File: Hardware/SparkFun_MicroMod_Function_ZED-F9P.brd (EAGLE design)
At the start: 38 x 65 mm, 126 parts, among them J2 MICROMOD_STANDARD, J3 QWIIC_RA, J4 U.FL, Q1 DMP21D0UT, U1 EEPROM, U2 U-BLOX_ZED-F9P, U3 FIN1017MXSOIC-8, U4 SN74AUP1T04DCK, U5 PCA9306DCUR, U6 74LVC541ABQ, U7 MIC5219 3.3V, U8 MIC5219 3.3V, U9 74LVC541ABQ

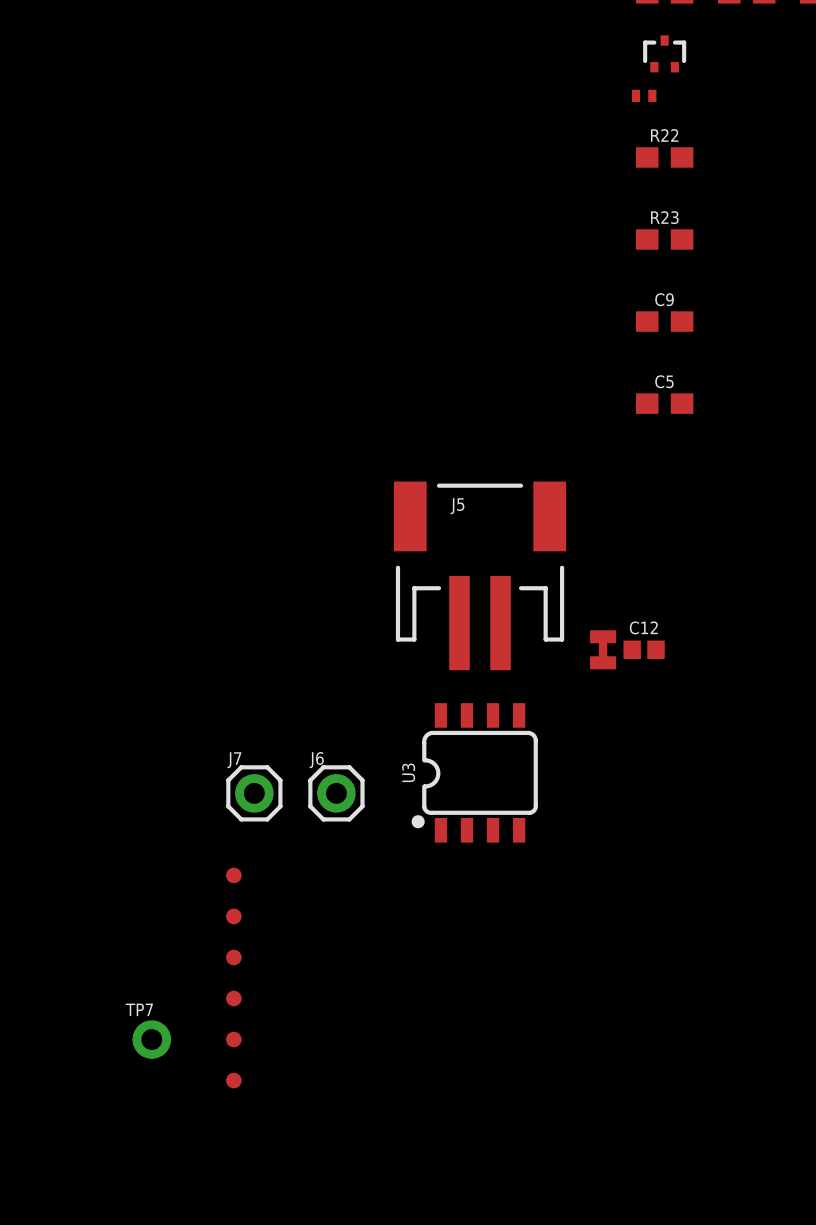
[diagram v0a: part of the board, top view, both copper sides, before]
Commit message: Changed power resistor, needed higher power rating.
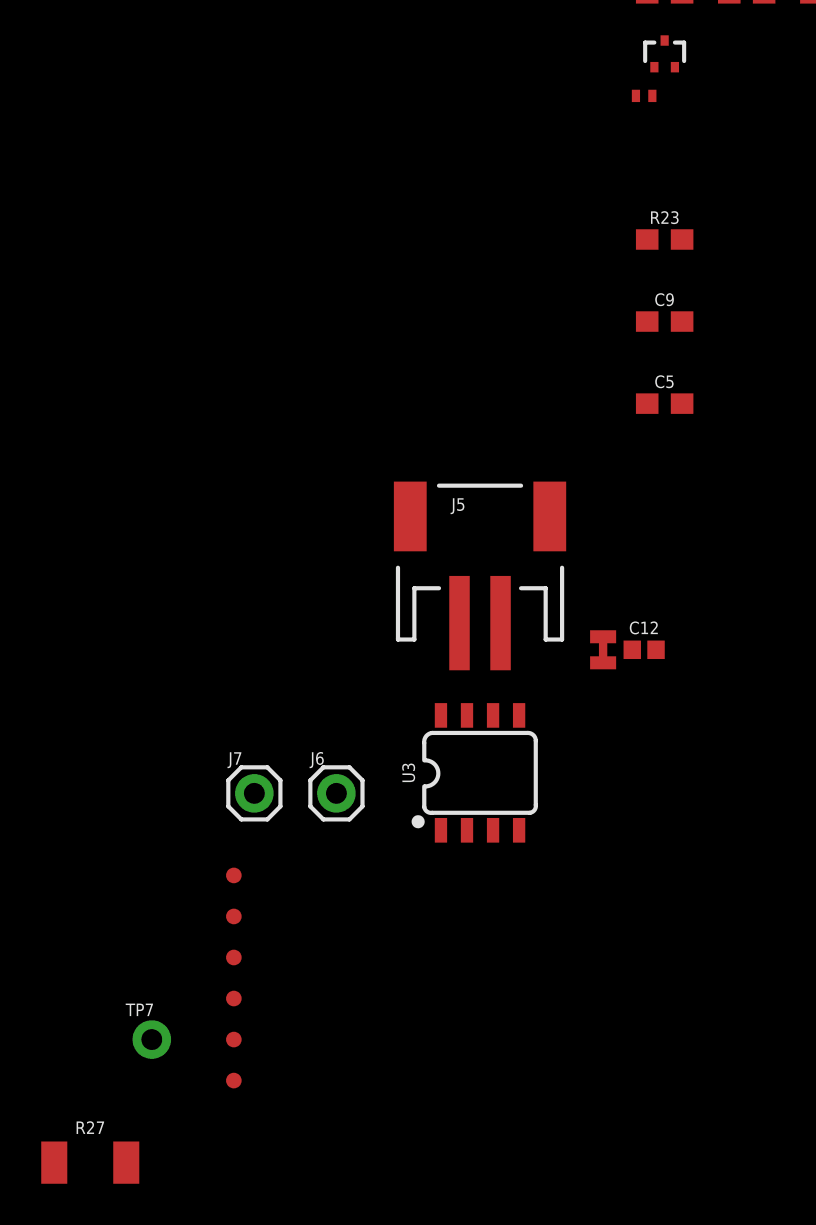
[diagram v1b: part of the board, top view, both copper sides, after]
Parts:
- removed R22: 20, SparkFun-Resistors:0603
- added R27: RK73H2ETTD16R9F, MicroMod_Function_GNSS_ublox_ZED_F9P:1210
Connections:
- net ANT_!SHORT!: now also R27.1; no longer R22.1
- net N$49: now also R27.2; no longer R22.2
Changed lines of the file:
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@@
 <attribute name="INDUCTANCE" value="150nH" x="-55" y="-966" size="1.778" layer="27" display="off"/>
-</element>
-<element name="R22" library="SparkFun-Resistors" package="0603" value="20" x="-54" y="-969" smashed="yes">
-<attribute name="NAME" x="-54" y="-968.238" size="0.6096" layer="25" font="vector" ratio="20" align="bottom-center"/>
-<attribute name="PROD_ID" value="RES-07862" x="-54" y="-969" size="1.778" layer="27" display="off"/>
-<attribute name="VALUE" x="-54" y="-969.762" size="0.6096" layer="27" font="vector" ratio="20" align="top-center"/>
 </element>
 <element name="R23" library="SparkFun-Resistors" package="0603" value="2.0k" x="-54" y="-973" smashed="yes">
@@
 <element name="TP19" library="SparkFun-Connectors" package="PAD.03X.03" value="TEST-POINT3" x="-83" y="141" smashed="yes"/>
 <element name="TP20" library="SparkFun-Connectors" package="PAD.03X.03" value="TEST-POINT3" x="-83" y="144" smashed="yes"/>
+<element name="R27" library="MicroMod_Function_GNSS_ublox_ZED_F9P" package="1210" value="RK73H2ETTD16R9F" x="-82" y="-1018" smashed="yes">
+<attribute name="NAME" x="-82" y="-1016.603" size="0.6096" layer="25" font="vector" ratio="20" align="bottom-center"/>
+<attribute name="POWER" value="0.5W" x="-82" y="-1018" size="1.778" layer="27" display="off"/>
+<attribute name="RESISTANCE" value="16.9" x="-82" y="-1018" size="1.778" layer="27" display="off"/>
+<attribute name="TOLERANCE" value="1%" x="-82" y="-1018" size="1.778" layer="27" display="off"/>
+<attribute name="VALUE" x="-82" y="-1019.397" size="0.6096" layer="27" font="vector" ratio="20" align="top-center"/>
+</element>
 </elements>
 <signals>
@@
 <contactref element="U6" pad="P$8"/>
 <contactref element="Q1" pad="P$1"/>
-<contactref element="R22" pad="1"/>
 <contactref element="R23" pad="2"/>
-<wire x1="-54.85" y1="-969" x2="-53.15" y2="-973" width="0" layer="19" extent="1-1"/>
-<wire x1="-54" y1="-963.3" x2="-54.85" y2="-969" width="0" layer="19" extent="1-1"/>
+<contactref element="R27" pad="1"/>
+<wire x1="-53.15" y1="-973" x2="-83.755" y2="-1018" width="0" layer="19" extent="1-1"/>
+<wire x1="-54" y1="-963.3" x2="-53.15" y2="-973" width="0" layer="19" extent="1-1"/>
 <wire x1="-28.75" y1="-480.35" x2="-54" y2="-963.3" width="0" layer="19" extent="1-1"/>
 </signal>
@@
 <contactref element="C13" pad="1"/>
 <contactref element="L1" pad="P$1"/>
-<contactref element="R22" pad="2"/>
+<contactref element="R27" pad="2"/>
 <wire x1="-43.5" y1="-961" x2="-52.05" y2="-955.6999" width="0" layer="19" extent="1-1"/>
 <wire x1="-55.4" y1="-966" x2="-52.05" y2="-955.6999" width="0" layer="19" extent="1-1"/>
-<wire x1="-53.15" y1="-969" x2="-55.4" y2="-966" width="0" layer="19" extent="1-1"/>
+<wire x1="-80.245" y1="-1018" x2="-55.4" y2="-966" width="0" layer="19" extent="1-1"/>
 </signal>
 <signal name="N$14">

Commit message: Update Post schematic review.
Made all easy changes, in midst of redoing decoupling per requests.
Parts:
- removed BYP, JP7, USB_EN: JUMPER-SMT_2_NO_SILK, SparkFun-Jumpers:SMT-JUMPER_2_NO_SILK
- removed C3, C5: 470pF, SparkFun-Capacitors:0603
- removed C4, C6: 2.2uF, SparkFun-Capacitors:0603
- removed D1, D12, D2, D8: RED, SparkFun-LED:LED-0603
- removed D10: 3A/10V/280mV, SparkFun-DiscreteSemi:SOD-323
- removed F1: 6V/2A, SparkFun-Fuses:1210
- removed JP10, JP2, JP3, JP8: JUMPER-SMT_2_NC_TRACE_SILK, SparkFun-Jumpers:SMT-JUMPER_2_NC_TRACE_SILK
- removed JP11, JP12: (no value), SparkFun-Jumpers:SMT-JUMPER_3_2-NC_TRACE_SILK
- removed R13, R14, R15, R16: 1.5k, SparkFun-Resistors:0603
- removed R17: 100k, SparkFun-Resistors:0603
- removed R19, R21, R4: 1k, SparkFun-Resistors:0603
- removed U$3, U$7: OPA344, SparkFun-IC-Amplifiers:SOT23-5
- removed U7, U8: MIC5219 3.3V, SparkFun-IC-Power:SOT23-5
- added C18: 2.2uF, SparkFun-Capacitors:0402-TIGHT
- added C19, C20: 0.1uF, SparkFun-Capacitors:0603
- added J8: Bus Selection, SparkFun-Connectors:1X03_LOCK
- added J9: (no value), SparkFun-Connectors:1X02
- added JP13: JUMPER-SMT_2_NO_SILK, SparkFun-Jumpers:SMT-JUMPER_2_NO_SILK
- added U$21, U$22: 74LVC4066D_QUAD_BILATERAL_SWITCH, SparkFun-IC-Logic:SO14
- added U10: OPA344, SparkFun-IC-Amplifiers:SOT23-5
- C11: device SparkFun-Capacitors:0402 -> SparkFun-Capacitors:0603
- J4: device SparkFun-RF:SMA-EDGE -> SparkFun-Connectors:U.FL
- J5: value (none) -> 455-1750-1-ND; device SparkFun-Connectors:JST-2-SMD -> SparkFun-Connectors:1X03
- J6: device SparkFun-Connectors:1X01 -> SparkFun-Connectors:1X04
- R10, R9: value 27OHM -> 27
- R27: value RK73H2ETTD16R9F -> 10; device MicroMod_Function_GNSS_ublox_ZED_F9P:1210 -> SparkFun-Resistors:0603
- R3: value 1k -> 10k
- U9: value 74LVC541ABQ -> SN74AUP1T04DCK; device MicroMod_Function_GNSS_ublox_ZED_F9P:DHVQFN20 -> MicroMod_Function_GNSS_ublox_ZED_F9P:SC-70-5_DCK
- moved TP1 1101.4 mm to (92.7, 84.6)
- moved TP2 1101.4 mm to (92.7, 82.6)
- moved TP3 1101.4 mm to (92.7, 80.6)
- moved TP4 1101.4 mm to (92.7, 78.6)
- moved TP5 1101.4 mm to (92.7, 76.6)
- moved TP6 1101.4 mm to (92.7, 74.6)
- moved TP7 1101.4 mm to (88.7, 76.6)
- moved U3 1077.8 mm to (52.2, 72.6)
- moved C12 1070.9 mm to (88.9, 68.2)
- moved SUPPLY35 1070.9 mm to (86.9, 68.2)
- moved C13 1058.3 mm to (92.3, 88.6)
- moved C7 1058.3 mm to (81.3, 109.6)
- moved C8 1058.3 mm to (97.3, 109.6)
- moved C9 1058.3 mm to (81.3, 72.6)
- moved L1 1058.3 mm to (80.3, 83.6)
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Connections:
- removed net GND2: JP10.2, JP2.2, JP3.2, JP4.1, JP5.1, JP6.1, JP8.2, JP9.2
- removed net N$11: D1.C, R3.2
- removed net N$14: C5.1, U8.4
- removed net N$15: JP8.1, R19.1
- removed net N$16: D8.C, R19.2
- removed net N$17: C3.1, U7.4
- removed net N$19: D10.A, USB_EN.2
- removed net N$20: BYP.1, D10.C, D9.C, F1.1
- removed net N$24: JP7.2, R17.1, U6.P$9
- removed net N$31: J2.70
- removed net N$33: J2.37
- removed net N$34: J2.35
- removed net N$35: J2.18
- removed net N$36: J2.16
- removed net N$37: J2.43
- removed net N$38: J2.41
- removed net N$39: JP10.1, R21.1
- removed net N$40: D12.C, R21.2
- removed net N$41: C15.1, D13.1, J4.SIG, L1.P$2
- removed net N$42: JP12.1, R14.2
- removed net N$43: JP11.1, R15.2
- removed net N$44: JP11.3, R16.2
- removed net N$47: JP12.3, R13.2
- removed net N$49: C13.1, L1.P$1, R27.2, U$7.4
- removed net N$50: J5.1, U3.7
- new net !ZED_DSEL!: U$22.12, U$22.13, U$22.5, U$22.6, U9.P$4
- new net PICO: U$22.10
- new net POCI: U$22.9
- new net RXI: U$21.10
- new net SCK: U$22.3
- new net SCL: U$21.3
- new net SDA: U$21.2
- new net SPI_!CS!: U$22.2
- new net TXO: U$21.9
- net !SAFEBOOT!: now also J7.1; no longer J2.57, U6.P$5
- net 3.3V: now also C2.1, U1.8; no longer D2.A, JP11.2
- net ANT_!SHORT!: now also C13.1, L1.P$1, R27.2, U10.4; no longer Q1.P$1, R23.2, R27.1, U6.P$8
- net ANT_DETECT: now also U10.1; no longer U$7.1, U6.P$7
- net ANT_OFF: no longer U9.P$18
- net EXTINT: now also J9.1, U6.P$5; no longer U6.P$6
- net GEO_STAT: now also U6.P$12; no longer U9.P$17
- net GND: now also C11.1, C19.2, C20.2, J5.3, J6.1, J6.4, J8.3, J9.2, JP13.1, JP4.1, JP5.1, JP6.1, JP9.2, U$21.7, U$22.7, U9.P$3; no longer C11.2, C3.2, C5.2, J1.SHLD1, J1.SHLD2, J1.SHLD3, J1.SHLD4, JP7.1, U7.2, U8.2, U9.P$10, U9.P$11, U9.P$21, U9.P$9
- net GND_RF: now also C18.2, J4.1, J4.2, U10.2; no longer C4.2, C6.2, J4.GND@0, J4.GND@1, J4.GND@2, J4.GND@3, U$3.2
- net IO_!OE!: no longer U9.P$1, U9.P$19
- net N$10: now also J8.1; no longer JP2.1
- net N$13: now also Q1.P$1, R23.2, R27.1; no longer C2.1, U1.8
- net N$18: now also J1.SHLD1, J1.SHLD2, J1.SHLD3, J1.SHLD4, JP13.2; no longer J2.38
- net N$48: now also U10.3; no longer U$7.3
- net N$51: now also J6.3; no longer J5.2
- net N$7: now also C15.1, D13.1, J4.FEED, L1.P$2; no longer D2.C, R4.2
- net N$9: now also J6.2, U3.7; no longer JP3.1, R4.1
- net PPS: now also U6.P$13; no longer U9.P$12
- net RTK_STAT: now also U6.P$11; no longer U9.P$16
- net RX/COPI: no longer U6.P$3
- net RX2/RTCM: now also J5.1; no longer J2.61, J6.1
- net SCL/SCK: no longer R16.1
- net SDA/!CS!: no longer R15.1
- net TX/CIPO: no longer U9.P$14
- net TX2/RTCM: now also J5.2, U6.P$17; no longer J2.59, J7.1, U9.P$15
- net TX_READY: now also U6.P$14; no longer U9.P$13
- net VCC: now also D9.C; no longer BYP.2, F1.2, U7.1, U7.3
- net VDD: now also C11.2, C19.1, C20.1, R3.2, U$21.14, U$22.14, U10.5, U9.P$5; no longer C11.1, C4.1, JP12.2, R17.2, U$3.5, U7.5, U8.3, U9.P$20
- net VIN: no longer D1.A
- net V_BATT: now also C18.1
- net V_USB: no longer D8.A, U8.1, USB_EN.1
- net V_USB_2: no longer C6.1, D12.A, U8.5
- net ZED_!SAFEBOOT!: no longer U6.P$15
- net ZED_ANT_!SHORT!: no longer U6.P$12
- net ZED_ANT_DETECT: no longer U6.P$13
- net ZED_ANT_OFF: no longer U9.P$2
- net ZED_DSEL: now also J8.2, U$21.12, U$21.13, U$21.5, U$21.6, U9.P$2; no longer U6.P$11
- net ZED_EXTINT: now also U6.P$15; no longer U6.P$14
- net ZED_GEO_STAT: now also U6.P$8; no longer U9.P$3
- net ZED_PPS: now also U6.P$7; no longer U9.P$8
- net ZED_RTK_STAT: now also U6.P$9; no longer U9.P$4
- net ZED_RX/COPI: no longer U6.P$17
- net ZED_SCL/SCK: no longer R14.1
- net ZED_SDA/!CS!: no longer R13.1
- net ZED_TX/CIPO: no longer U9.P$6
- net ZED_TX2/RTCM: now also U6.P$3; no longer U9.P$5
- net ZED_TX_READY: now also U6.P$6; no longer U9.P$7
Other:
- outline, holes or cut-outs redrawn

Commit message: Complete schematic after DR changes.
Reorganized power: changed supply, removed fuse, replaced usb_det supply with voltage divider, renamed power nets.
Added TPs and PTH breakouts for some pins.
Changed I/O decoupling: Replaced octal buffer with 2x quad SSR switches, removed buffer on antenna supervision, rearranged pins on remaining octal buffer.
Labeled diff PPS signal.
Added second Qwiic connector.
Added selector headers for bus and antenna supervisor circuits.
Removed extra LEDs.
Replaced SMA with u.FL.
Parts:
- removed C16: 0.1uF, SparkFun-Capacitors:0603
- removed D5: BLUE, SparkFun-LED:LED-0603
- removed JP6: JUMPER-SMT_2_NC_TRACE_SILK, SparkFun-Jumpers:SMT-JUMPER_2_NC_TRACE_SILK
- removed R25: 10k, SparkFun-Resistors:0603
- removed R26: DNP, SparkFun-Resistors:0603_NO_CREAM
- removed TP11: TEST-POINT3, SparkFun-Connectors:PAD.03X.03
- removed U$21, U$22: 74LVC4066D_QUAD_BILATERAL_SWITCH, SparkFun-IC-Logic:SO14
- added C3: 1.0uF, SparkFun-Capacitors:0603
- added D1: 3A/10V/280mV, SparkFun-DiscreteSemi:SOD-323
- added J10: QWIIC_RA, SparkFun-Connectors:JST04_1MM_RA
- added J11: Bus Selection, SparkFun-Connectors:1X03_LOCK
- added J12: USB Female Type C Connector, SparkFun-Connectors:USB-C-16P-4LAYER-ISOLATED
- added J13, J14, J15, J16, J17: (no value), SparkFun-Connectors:1X01
- added J18: (no value), SparkFun-Connectors:1X02
- added JP2: JUMPER-SMT_2_NO_SILK, SparkFun-Jumpers:SMT-JUMPER_2_NO_SILK
- added R4: 10k, SparkFun-Resistors:0603
- added U11, U12: 74LVC4066D_QUAD_BILATERAL_SWITCH, SparkFun-IC-Logic:SO14
- added U7: 3.3V, SparkFun-IC-Power:SOT23-5
- C1: value 10pF -> 1.0uF
- J1: device SparkFun-Connectors:USB-C-16P-2LAYER-PADS -> SparkFun-Connectors:1X01
- R12: value 220k -> 68.1k
- R7: value 1k -> 10k
- TP7, TP9: value TEST-POINTPOGO_PTH -> TEST-POINT3; device SparkFun-Connectors:1X01_NO_SILK -> SparkFun-Connectors:PAD.03X.03
- U5: value PCA9306DCUR -> SN74LVC1G66DRYR; device MicroMod_Function_GNSS_ublox_ZED_F9P:VSSOP-8_DCU -> MicroMod_Function_GNSS_ublox_ZED_F9P:USON_DRY0006A
- moved TP20 314.2 mm to (-50.6, -182.3)
- moved TP10 310.6 mm to (-50.6, -198.1)
- moved TP19 309.4 mm to (-50.6, -180.2)
- moved TP8 308.9 mm to (-48.5, -190.2)
- moved TP2 306.3 mm to (-50.6, -188.1)
- moved TP9 301.5 mm to (-50.6, -192.3)
- moved TP7 301.0 mm to (-50.6, -190.2)
- moved TP1 299.2 mm to (-50.6, -178.1)
- moved TP6 298.2 mm to (-48.5, -188.1)
- moved U5 298.1 mm to (-24.4, -157.6)
- moved C10 284.4 mm to (-21.8, -157.5)
- moved R12 272.5 mm to (-23.6, -167.4)
- moved R7 271.4 mm to (-21.5, -154.2)
- moved J1 236.6 mm to (-30.4, -174.7), turned to 0 degrees
- moved JP13 125.8 mm to (-17.8, -133.1)
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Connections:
- removed net N$18: J1.SHLD1, J1.SHLD2, J1.SHLD3, J1.SHLD4, JP13.2
- removed net N$45: JP6.2, R7.1
- removed net N$46: D5.C, R7.2
- removed net PICO: U$22.10
- removed net POCI: U$22.9
- removed net RX/COPI: J2.15, J2.5, TP15.1
- removed net RXI: U$21.10
- removed net SCK: U$22.3
- removed net SCL: U$21.3
- removed net SCL/SCK: J2.21, J2.3, J3.4, TP19.1, U1.6, U5.P$3
- removed net SDA: U$21.2
- removed net SDA/!CS!: J2.19, J2.49, J3.3, TP20.1, U1.5, U5.P$4
- removed net SPI_!CS!: U$22.2
- removed net TX/CIPO: J2.13, J2.7, TP16.1
- removed net TXO: U$21.9
- removed net VCC: C12.1, D9.C, TP6.1, U3.1
- removed net V_USB_2: C7.1, C8.1, R18.2, TP11.1, U2.38
- new net 5V: C3.1, D1.C, D9.C, U5.P$4, U5.P$6, U7.1
- new net MM_!CS!: J2.49, TP8.1, U12.2
- new net MM_CIPO: J2.7, TP6.1, U12.9
- new net MM_COPI: J2.5, TP2.1, U12.10
- new net MM_RX: J2.15, TP15.1, U11.10
- new net MM_SCK: J2.3, TP7.1, U12.3
- new net MM_SCL: J10.4, J2.21, J3.4, TP19.1, U1.6, U11.3
- new net MM_SDA: J10.3, J2.19, J3.3, TP20.1, U1.5, U11.2
- new net MM_TX: J2.13, TP16.1, U11.9
- new net N$11: J11.1, R4.1
- new net N$16: D1.A, JP2.2
- new net SHLD: J12.SHLD1, J12.SHLD2, J12.SHLD3, J12.SHLD4, J12.SHLD5, J12.SHLD6, J12.SHLD7, J12.SHLD8, JP13.1
- new net V_ZED: C10.1, C11.2, C14.2, C17.2, C19.1, C20.1, C9.1, D11.A, U10.5, U11.14, U12.14, U2.33, U2.34, U4.P$2, U4.P$5, U6.P$20, U9.P$5
- new net ZED_USB_DET: C7.1, C8.1, R12.1, R12.2, R18.2, U2.38, U5.P$2
- net !RESET!: now also J18.1, U6.P$3; no longer U6.P$4
- net !ZED_DSEL!: now also U12.12, U12.13, U12.5, U12.6; no longer U$22.12, U$22.13, U$22.5, U$22.6
- net 3.3V: now also C12.1, J10.2, U3.1; no longer C16.1, TP8.1, U5.P$2
- net ANT_OFF: now also J11.2; no longer R25.2, R26.1
- net EXTINT: now also TP10.1, U6.P$4; no longer U6.P$5
- net GEO_STAT: now also J2.57, U6.P$11; no longer D5.A, U6.P$12
- net GND: now also C3.2, J10.1, J12.GND, J12.GND2, J13.1, J14.1, J18.2, JP13.2, U5.P$3, U7.2; no longer C10.2, C11.1, C16.2, C17.1, C19.2, C20.2, J1.GND, J1.GND2, J8.3, JP13.1, JP6.1, TP2.1, TP7.1, U$21.7, U$22.7, U4.P$3, U5.P$1, U6.P$10, U6.P$21, U9.P$3
- net GND_RF: now also C10.2, C11.1, C17.1, C19.2, C20.2, J15.1, J16.1, J8.3, R7.1, U11.7, U12.7, U4.P$3, U6.P$10, U6.P$21, U9.P$3; no longer R25.1, TP9.1
- net N$1: now also J12.A6, J12.B6; no longer J1.A6, J1.B6
- net N$12: now also J11.3, R7.2; no longer C1.1, R12.1, U5.P$7, U5.P$8
- net N$2: now also J12.A7, J12.B7; no longer J1.A7, J1.B7
- net N$3: now also J12.B5; no longer J1.B5
- net N$4: now also J12.A5; no longer J1.A5
- net PPS: now also U6.P$18; no longer U6.P$13
- net PWR_EN: now also U7.3
- net RTK_STAT: now also J2.59, U6.P$12; no longer U6.P$11
- net RX2/RTCM: now also U6.P$7; no longer U6.P$2
- net TX2/RTCM: now also U6.P$14; no longer U6.P$17
- net TX_READY: now also TP9.1, U6.P$15; no longer U6.P$14
- net VDD: now also C1.1, J1.1, U7.5; no longer C10.1, C11.2, C14.2, C17.2, C19.1, C20.1, C9.1, D11.A, R12.2, U$21.14, U$22.14, U10.5, U2.33, U2.34, U4.P$2, U4.P$5, U6.P$20, U9.P$5
- net V_BATT: now also J17.1
- net V_RF: now also R4.2; no longer R26.2
- net V_USB: now also J12.VBUS1, J12.VBUS2, JP2.1, U5.P$1; no longer J1.VBUS1, J1.VBUS2, TP10.1
- net ZED_!RESET!: now also U6.P$17; no longer U6.P$16
- net ZED_DSEL: now also U11.12, U11.13, U11.5, U11.6; no longer U$21.12, U$21.13, U$21.5, U$21.6
- net ZED_EXTINT: now also U6.P$16; no longer U6.P$15
- net ZED_GEO_STAT: now also U6.P$9; no longer U6.P$8
- net ZED_PPS: now also U6.P$2; no longer U6.P$7
- net ZED_RTK_STAT: now also U6.P$8; no longer U6.P$9
- net ZED_RX/COPI: now also U11.11, U12.11
- net ZED_RX2/RTCM: now also U6.P$13; no longer U6.P$18
- net ZED_SCL/SCK: now also U11.4, U12.4; no longer U5.P$6
- net ZED_SDA/!CS!: now also U11.1, U12.1; no longer U5.P$5
- net ZED_TX/CIPO: now also U11.8, U12.8
- net ZED_TX2/RTCM: now also U6.P$6; no longer U6.P$3
- net ZED_TX_READY: now also U6.P$5; no longer U6.P$6
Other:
- outline, holes or cut-outs redrawn
